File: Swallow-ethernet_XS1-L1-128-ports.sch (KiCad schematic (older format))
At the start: 13 parts, among them U11 XS1-L1-128

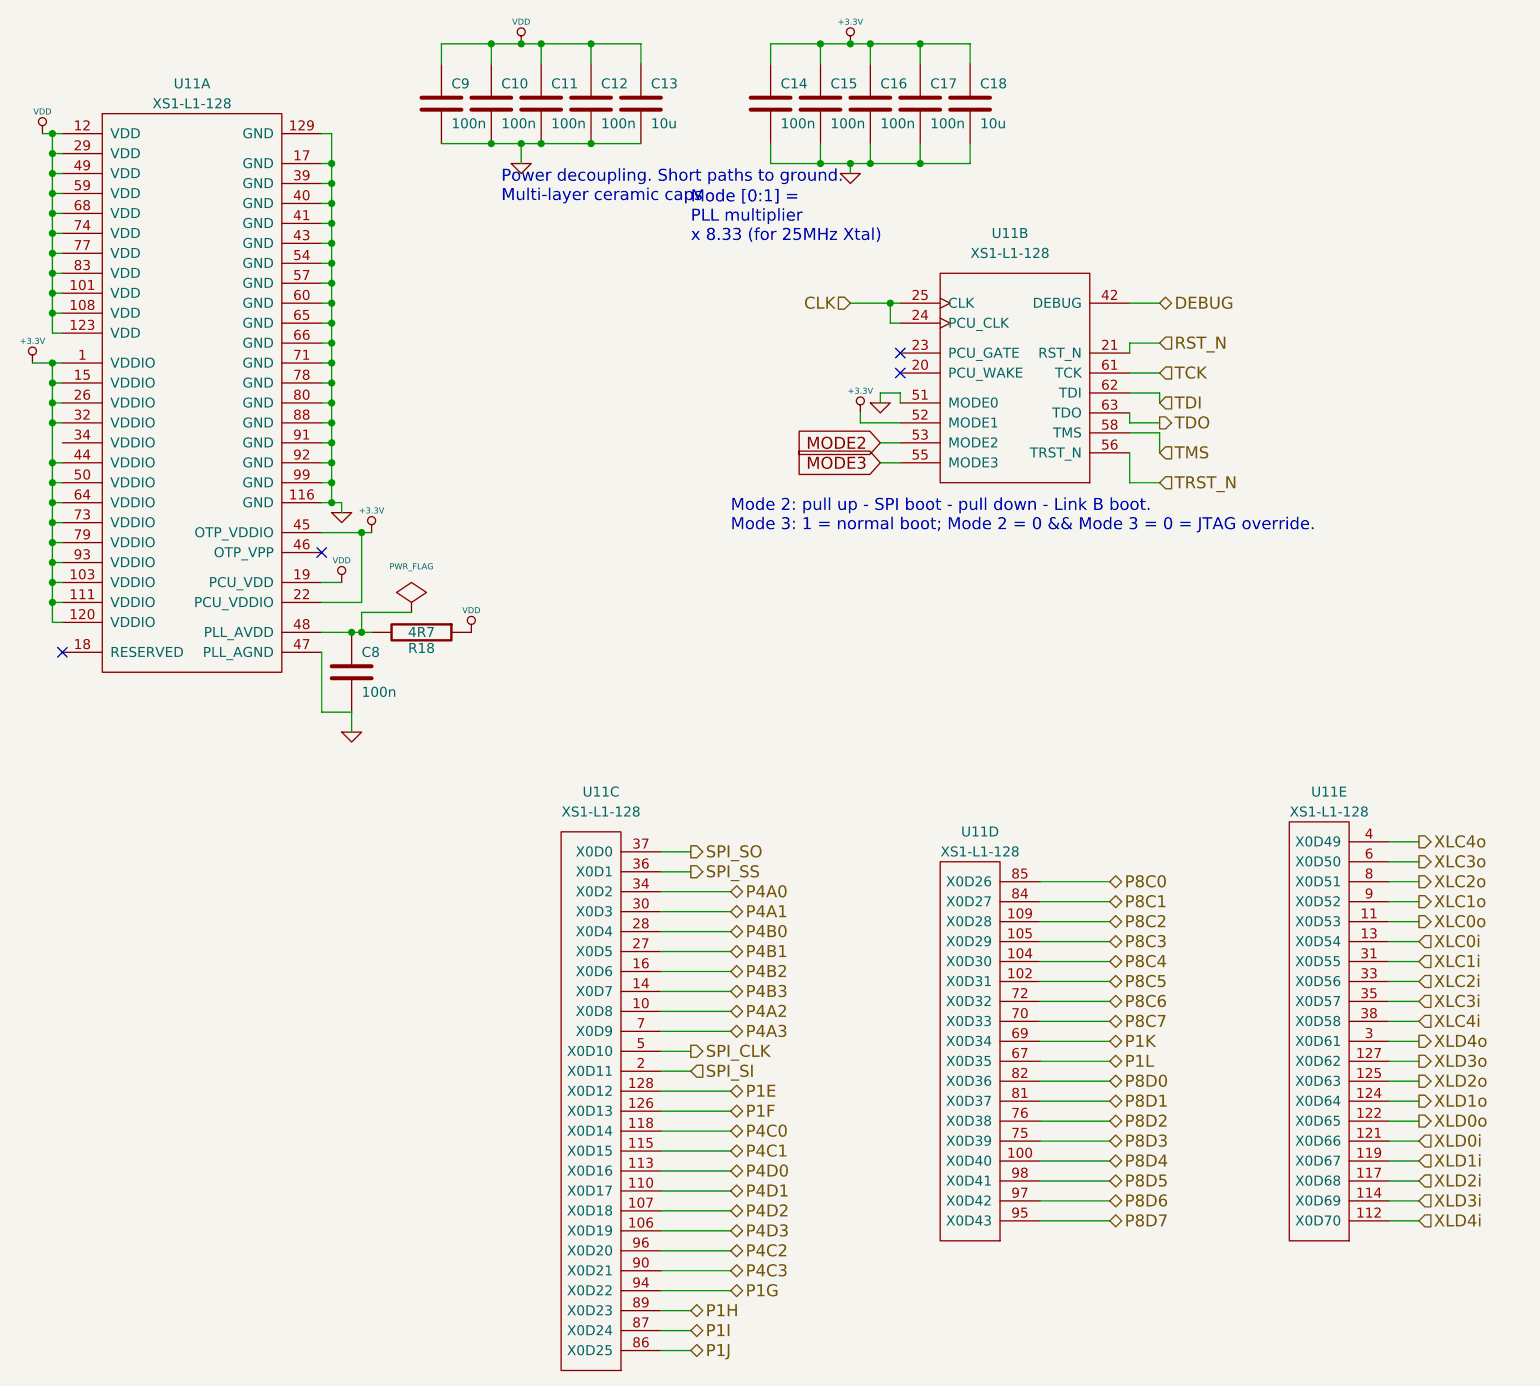
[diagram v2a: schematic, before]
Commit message: Re-annotated schematic and deleted redundant components from PCB design.
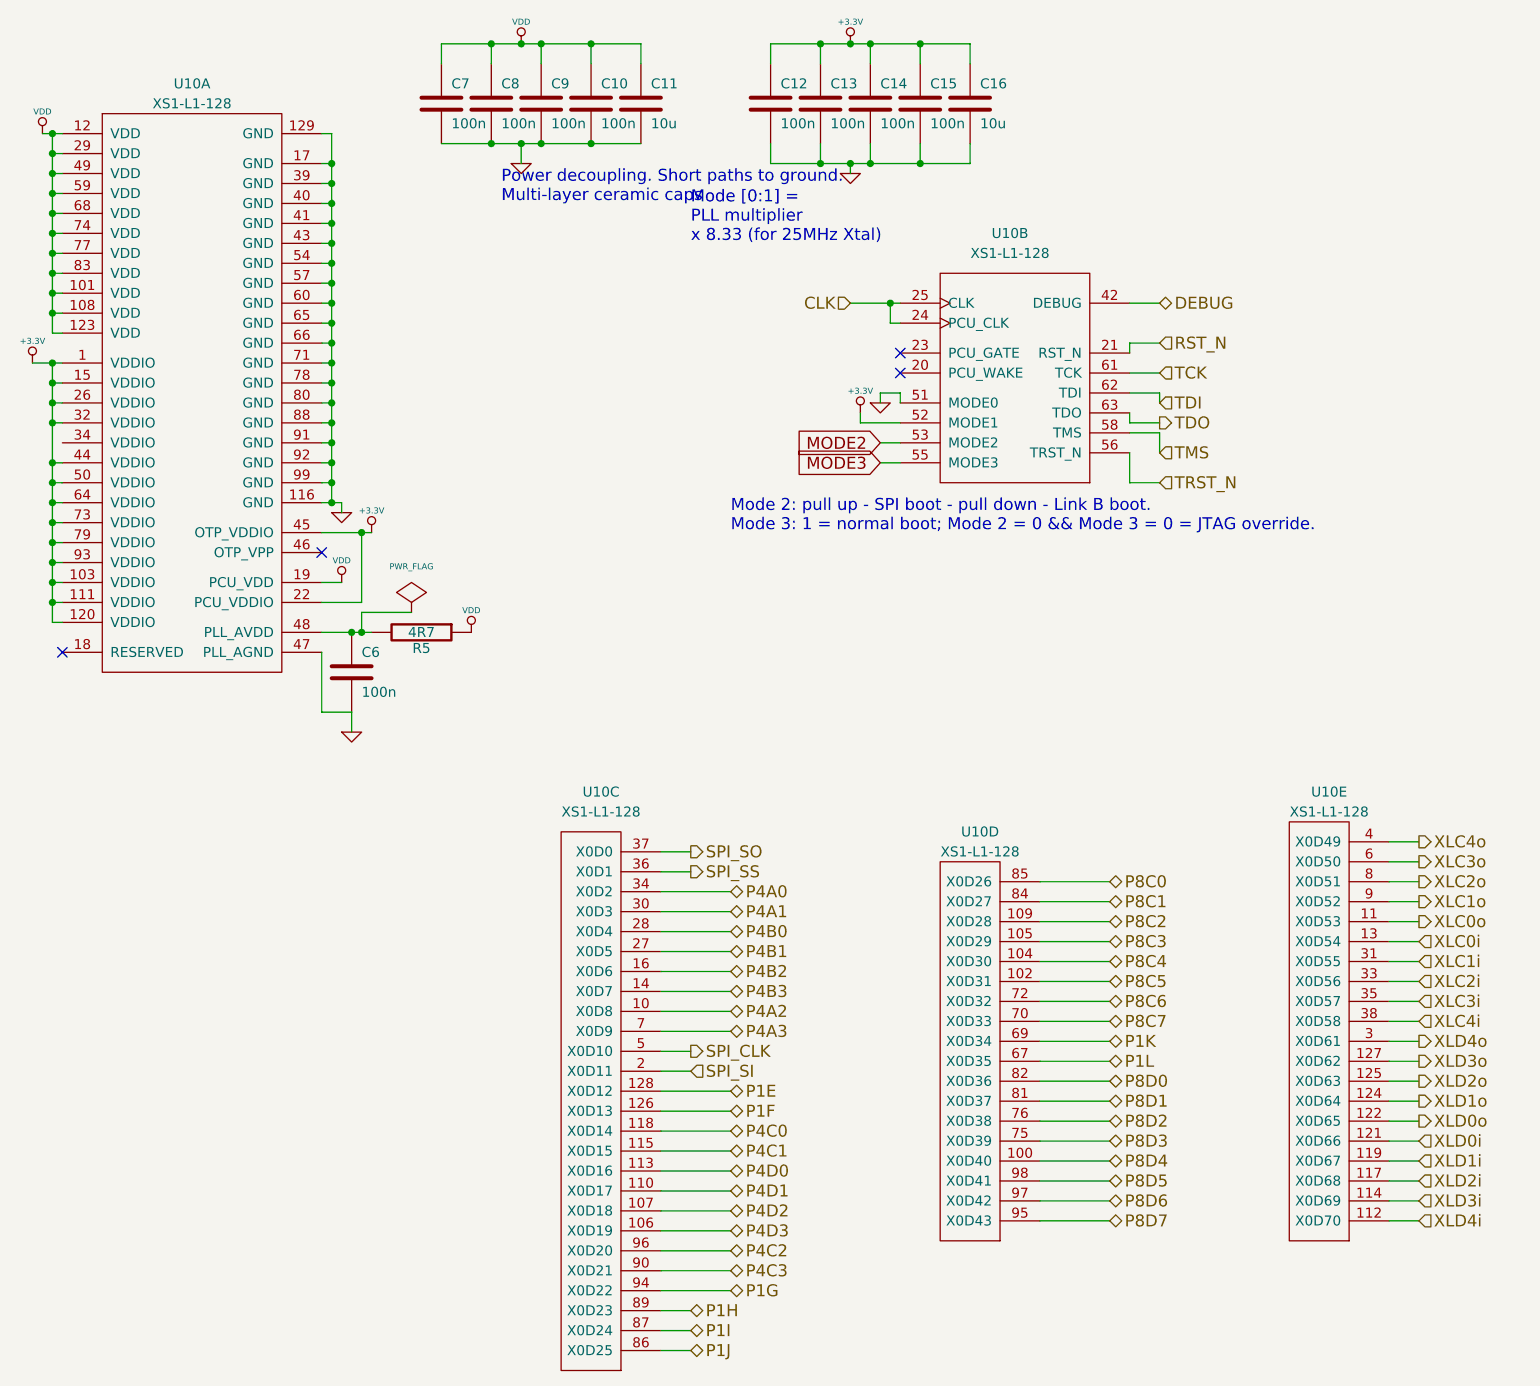
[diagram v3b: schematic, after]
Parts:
- renumbered C12 to C10, C13 to C11, C14 to C12, C15 to C13, C16 to C14, C17 to C15, C18 to C16, C8 to C6, C9 to C7, C10 to C8, C11 to C9, R18 to R5, U11 to U10
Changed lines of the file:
@@
-EESchema Schematic File Version 2  date 30/09/2012 22:11:50
+EESchema Schematic File Version 2  date 30/09/2012 22:23:08
 LIBS:power
 LIBS:device
@@
 Mode [0:1] =\nPLL multiplier\nx 8.33 (for 25MHz Xtal)
 $Comp
-L GND #PWR071
+L GND #PWR047
 U 1 1 4F5B945A
 P 5400 2700
-F 0 "#PWR071" H 5400 2700 30  0001 C CNN
+F 0 "#PWR047" H 5400 2700 30  0001 C CNN
 F 1 "GND" H 5400 2630 30  0001 C CNN
 	1    5400 2700
@@
 MODE3
 $Comp
-L PWR_FLAG #FLG072
+L PWR_FLAG #FLG048
 U 1 1 4ED164B1
 P 3050 3750
-F 0 "#FLG072" H 3050 4020 30  0001 C CNN
+F 0 "#FLG048" H 3050 4020 30  0001 C CNN
 F 1 "PWR_FLAG" H 3050 3980 30  0000 C CNN
 	1    3050 3750
@@
 TRST_N
 $Comp
-L C C18
+L C C16
 U 1 1 4ECE485F
 P 5850 1200
-F 0 "C18" H 5900 1300 50  0000 L CNN
+F 0 "C16" H 5900 1300 50  0000 L CNN
 F 1 "10u" H 5900 1100 50  0000 L CNN
 F 2 "SM0805" H 5850 1200 60  0001 C CNN
@@
 $EndComp
 $Comp
-L C C13
+L C C11
 U 1 1 4ECE4845
 P 4200 1200
-F 0 "C13" H 4250 1300 50  0000 L CNN
+F 0 "C11" H 4250 1300 50  0000 L CNN
 F 1 "10u" H 4250 1100 50  0000 L CNN
 F 2 "SM0805" H 4200 1200 60  0001 C CNN
@@
 Power decoupling. Short paths to ground.\nMulti-layer ceramic caps
 $Comp
-L GND #PWR073
+L GND #PWR049
 U 1 1 4ECE47A2
 P 3600 1500
-F 0 "#PWR073" H 3600 1500 30  0001 C CNN
+F 0 "#PWR049" H 3600 1500 30  0001 C CNN
 F 1 "GND" H 3600 1430 30  0001 C CNN
 	1    3600 1500
@@
 $EndComp
 $Comp
-L GND #PWR074
+L GND #PWR050
 U 1 1 4ECE479D
 P 5250 1550
-F 0 "#PWR074" H 5250 1550 30  0001 C CNN
+F 0 "#PWR050" H 5250 1550 30  0001 C CNN
 F 1 "GND" H 5250 1480 30  0001 C CNN
 	1    5250 1550
@@
 $EndComp
 $Comp
-L VDD #PWR075
+L VDD #PWR051
 U 1 1 4ECE4775
 P 3600 900
-F 0 "#PWR075" H 3600 1000 30  0001 C CNN
+F 0 "#PWR051" H 3600 1000 30  0001 C CNN
 F 1 "VDD" H 3600 1010 30  0000 C CNN
 	1    3600 900
@@
 $EndComp
 $Comp
-L +3.3V #PWR076
+L +3.3V #PWR052
 U 1 1 4ECE476D
 P 5250 900
-F 0 "#PWR076" H 5250 860 30  0001 C CNN
+F 0 "#PWR052" H 5250 860 30  0001 C CNN
 F 1 "+3.3V" H 5250 1010 30  0000 C CNN
 	1    5250 900
@@
 $EndComp
 $Comp
-L C C17
+L C C15
 U 1 1 4ECE4762
 P 5600 1200
-F 0 "C17" H 5650 1300 50  0000 L CNN
+F 0 "C15" H 5650 1300 50  0000 L CNN
 F 1 "100n" H 5650 1100 50  0000 L CNN
 F 2 "SM0603" H 5600 1200 60  0001 C CNN
@@
 $EndComp
 $Comp
-L C C16
+L C C14
 U 1 1 4ECE475F
 P 5350 1200
-F 0 "C16" H 5400 1300 50  0000 L CNN
+F 0 "C14" H 5400 1300 50  0000 L CNN
 F 1 "100n" H 5400 1100 50  0000 L CNN
 F 2 "SM0603" H 5350 1200 60  0001 C CNN
@@
 $EndComp
 $Comp
-L C C15
+L C C13
 U 1 1 4ECE475C
 P 5100 1200
-F 0 "C15" H 5150 1300 50  0000 L CNN
+F 0 "C13" H 5150 1300 50  0000 L CNN
 F 1 "100n" H 5150 1100 50  0000 L CNN
 F 2 "SM0603" H 5100 1200 60  0001 C CNN
@@
 $EndComp
 $Comp
-L C C14
+L C C12
 U 1 1 4ECE4757
 P 4850 1200
-F 0 "C14" H 4900 1300 50  0000 L CNN
+F 0 "C12" H 4900 1300 50  0000 L CNN
 F 1 "100n" H 4900 1100 50  0000 L CNN
 F 2 "SM0603" H 4850 1200 60  0001 C CNN
@@
 $EndComp
 $Comp
-L C C12
+L C C10
 U 1 1 4ECE4753
 P 3950 1200
-F 0 "C12" H 4000 1300 50  0000 L CNN
+F 0 "C10" H 4000 1300 50  0000 L CNN
 F 1 "100n" H 4000 1100 50  0000 L CNN
 F 2 "SM0603" H 3950 1200 60  0001 C CNN
@@
 $EndComp
 $Comp
-L C C11
+L C C9
 U 1 1 4ECE4750
 P 3700 1200
-F 0 "C11" H 3750 1300 50  0000 L CNN
+F 0 "C9" H 3750 1300 50  0000 L CNN
 F 1 "100n" H 3750 1100 50  0000 L CNN
 F 2 "SM0603" H 3700 1200 60  0001 C CNN
@@
 $EndComp
 $Comp
-L C C10
+L C C8
 U 1 1 4ECE474B
 P 3450 1200
-F 0 "C10" H 3500 1300 50  0000 L CNN
+F 0 "C8" H 3500 1300 50  0000 L CNN
 F 1 "100n" H 3500 1100 50  0000 L CNN
 F 2 "SM0603" H 3450 1200 60  0001 C CNN
@@
 $EndComp
 $Comp
-L C C9
+L C C7
 U 1 1 4ECE4733
 P 3200 1200
-F 0 "C9" H 3250 1300 50  0000 L CNN
+F 0 "C7" H 3250 1300 50  0000 L CNN
 F 1 "100n" H 3250 1100 50  0000 L CNN
 F 2 "SM0603" H 3200 1200 60  0001 C CNN
@@
 NoConn ~ 2600 3450
 $Comp
-L VDD #PWR077
+L VDD #PWR053
 U 1 1 4ECE4690
 P 2700 3600
-F 0 "#PWR077" H 2700 3700 30  0001 C CNN
+F 0 "#PWR053" H 2700 3700 30  0001 C CNN
 F 1 "VDD" H 2700 3710 30  0000 C CNN
 	1    2700 3600
@@
 $EndComp
 $Comp
-L +3.3V #PWR078
+L +3.3V #PWR054
 U 1 1 4ECE4673
 P 2850 3350
-F 0 "#PWR078" H 2850 3310 30  0001 C CNN
+F 0 "#PWR054" H 2850 3310 30  0001 C CNN
 F 1 "+3.3V" H 2850 3460 30  0000 C CNN
 	1    2850 3350
@@
 TDI
 $Comp
-L +3.3V #PWR079
+L +3.3V #PWR055
 U 1 1 4ECE416A
 P 5300 2750
-F 0 "#PWR079" H 5300 2710 30  0001 C CNN
+F 0 "#PWR055" H 5300 2710 30  0001 C CNN
 F 1 "+3.3V" H 5300 2860 30  0000 C CNN
 	1    5300 2750
@@
 $EndComp
 $Comp
-L GND #PWR080
+L GND #PWR056
 U 1 1 4ECE3EA5
 P 2750 4350
-F 0 "#PWR080" H 2750 4350 30  0001 C CNN
+F 0 "#PWR056" H 2750 4350 30  0001 C CNN
 F 1 "GND" H 2750 4280 30  0001 C CNN
 	1    2750 4350
@@
 $EndComp
 $Comp
-L VDD #PWR081
+L VDD #PWR057
 U 1 1 4ECE3EA2
 P 3350 3850
-F 0 "#PWR081" H 3350 3950 30  0001 C CNN
+F 0 "#PWR057" H 3350 3950 30  0001 C CNN
 F 1 "VDD" H 3350 3960 30  0000 C CNN
 	1    3350 3850
@@
 $EndComp
 $Comp
-L R R18
+L R R5
 U 1 1 4ECE3E9B
 P 3100 3850
-F 0 "R18" V 3180 3850 50  0000 C CNN
+F 0 "R5" V 3180 3850 50  0000 C CNN
 F 1 "4R7" V 3100 3850 50  0000 C CNN
 F 2 "SM0402" H 3100 3850 60  0001 C CNN
@@
 $EndComp
 $Comp
-L C C8
+L C C6
 U 1 1 4ECE3E71
 P 2750 4050
-F 0 "C8" H 2800 4150 50  0000 L CNN
+F 0 "C6" H 2800 4150 50  0000 L CNN
 F 1 "100n" H 2800 3950 50  0000 L CNN
 F 2 "SM0603" H 2750 4050 60  0001 C CNN
@@
 P8C4
 $Comp
-L GND #PWR082
+L GND #PWR058
 U 1 1 4ECE33A4
 P 2700 3250
-F 0 "#PWR082" H 2700 3250 30  0001 C CNN
+F 0 "#PWR058" H 2700 3250 30  0001 C CNN
 F 1 "GND" H 2700 3180 30  0001 C CNN
 	1    2700 3250
@@
 $EndComp
 $Comp
-L VDD #PWR083
+L VDD #PWR059
 U 1 1 4ECE3345
 P 1200 1350
-F 0 "#PWR083" H 1200 1450 30  0001 C CNN
+F 0 "#PWR059" H 1200 1450 30  0001 C CNN
 F 1 "VDD" H 1200 1460 30  0000 C CNN
 	1    1200 1350
@@
 $EndComp
 $Comp
-L +3.3V #PWR084
+L +3.3V #PWR060
 U 1 1 4ECE3320
 P 1150 2500
-F 0 "#PWR084" H 1150 2460 30  0001 C CNN
+F 0 "#PWR060" H 1150 2460 30  0001 C CNN
 F 1 "+3.3V" H 1150 2610 30  0000 C CNN
 	1    1150 2500
@@
 AR Path="/4ECE31E2" Ref="U?"  Part="5"
 AR Path="/4F5A23DA/4ECE31E2" Ref="U?"  Part="5"
-AR Path="/4F5A2605/4F5A264B/4ECE31E2" Ref="U11"  Part="5"
-F 0 "U11" H 7650 7250 50  0000 C CNN
+AR Path="/4F5A2605/4F5A264B/4ECE31E2" Ref="U10"  Part="5"
+F 0 "U10" H 7650 7250 50  0000 C CNN
 F 1 "XS1-L1-128" H 7650 7150 50  0000 C CNN
 F 2 "XMOS_X1-L1_128TQFP" H 7650 5950 60  0001 C CNN
@@
 AR Path="/4ECE31D9" Ref="U?"  Part="4"
 AR Path="/4F5A23DA/4ECE31D9" Ref="U?"  Part="4"
-AR Path="/4F5A2605/4F5A264B/4ECE31D9" Ref="U11"  Part="4"
-F 0 "U11" H 5900 7450 50  0000 C CNN
+AR Path="/4F5A2605/4F5A264B/4ECE31D9" Ref="U10"  Part="4"
+F 0 "U10" H 5900 7450 50  0000 C CNN
 F 1 "XS1-L1-128" H 5900 7350 50  0000 C CNN
 F 2 "XMOS_X1-L1_128TQFP" H 5900 6150 60  0001 C CNN
@@
 AR Path="/4ECE31CA" Ref="U?"  Part="3"
 AR Path="/4F5A23DA/4ECE31CA" Ref="U?"  Part="3"
-AR Path="/4F5A2605/4F5A264B/4ECE31CA" Ref="U11"  Part="3"
-F 0 "U11" H 4000 7250 50  0000 C CNN
+AR Path="/4F5A2605/4F5A264B/4ECE31CA" Ref="U10"  Part="3"
+F 0 "U10" H 4000 7250 50  0000 C CNN
 F 1 "XS1-L1-128" H 4000 7150 50  0000 C CNN
 F 2 "XMOS_X1-L1_128TQFP" H 4000 5950 60  0001 C CNN
@@
 AR Path="/4ECE31BE" Ref="U?"  Part="2"
 AR Path="/4F5A23DA/4ECE31BE" Ref="U?"  Part="2"
-AR Path="/4F5A2605/4F5A264B/4ECE31BE" Ref="U11"  Part="2"
-F 0 "U11" H 6050 4450 50  0000 C CNN
+AR Path="/4F5A2605/4F5A264B/4ECE31BE" Ref="U10"  Part="2"
+F 0 "U10" H 6050 4450 50  0000 C CNN
 F 1 "XS1-L1-128" H 6050 4350 50  0000 C CNN
 F 2 "XMOS_X1-L1_128TQFP" H 6050 3150 60  0001 C CNN
@@
 AR Path="/4ECE3082" Ref="U?"  Part="1"
 AR Path="/4F5A23DA/4ECE3082" Ref="U?"  Part="1"
-AR Path="/4F5A2605/4F5A264B/4ECE3082" Ref="U11"  Part="1"
-F 0 "U11" H 1950 3700 50  0000 C CNN
+AR Path="/4F5A2605/4F5A264B/4ECE3082" Ref="U10"  Part="1"
+F 0 "U10" H 1950 3700 50  0000 C CNN
 F 1 "XS1-L1-128" H 1950 3600 50  0000 C CNN
 F 2 "XMOS_X1-L1_128TQFP" H 1950 2400 60  0001 C CNN
